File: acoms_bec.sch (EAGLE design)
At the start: 9 parts, among them IC1 NJU7201L35, Q1 2SC2458, Q2 MJB45H11

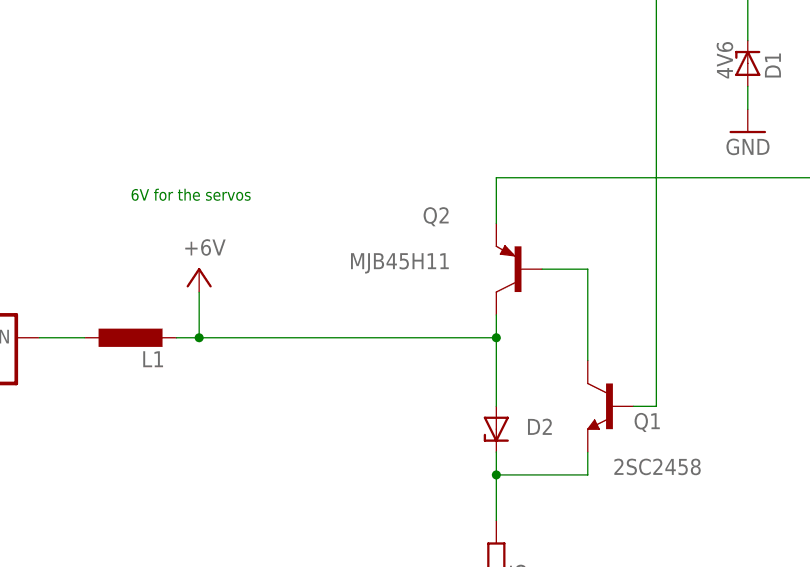
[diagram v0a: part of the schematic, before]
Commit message: Transistor name update to the original
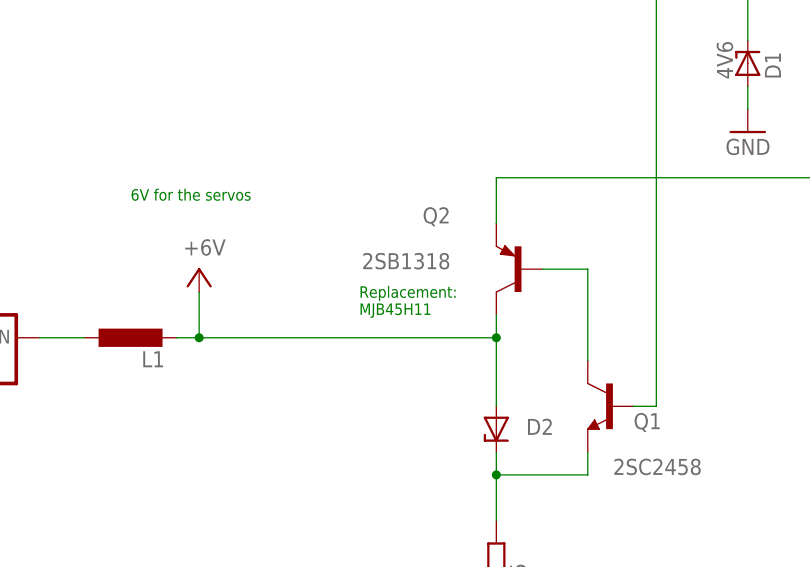
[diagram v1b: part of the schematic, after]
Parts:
- Q2: value MJB45H11 -> 2SB1318
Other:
- note added: "Replacement: MJB45H11"
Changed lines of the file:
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@@
 <part name="GND4" library="supply1" deviceset="GND" device=""/>
 <part name="Q1" library="dp_devices" deviceset="TRANSISTOR_BJT_NPN" device="-TO-92-ECB" value="2SC2458"/>
-<part name="Q2" library="dp_devices" deviceset="TRANSISTOR_BJT_PNP" device="-TO-92-ECB" value="MJB45H11"/>
+<part name="Q2" library="dp_devices" deviceset="TRANSISTOR_BJT_PNP" device="-TO-92-ECB" value="2SB1318"/>
 <part name="R2" library="rcl" deviceset="R-EU_" device="0309/V" value="395"/>
 <part name="GND5" library="supply1" deviceset="GND" device=""/>
@@
 <text x="93.98" y="91.44" size="1.27" layer="91" font="vector">6V for the servos</text>
 <text x="198.12" y="114.3" size="1.27" layer="91" font="vector">BATT conncetor</text>
+<text x="119.38" y="78.74" size="1.27" layer="91">Replacement:
+MJB45H11</text>
 </plain>
 <instances>
